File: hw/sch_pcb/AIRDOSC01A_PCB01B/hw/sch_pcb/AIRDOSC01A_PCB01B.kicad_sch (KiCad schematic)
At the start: 39 parts, among them J1 HEADER_2x01_PARALLEL, J10 HEADER_2x01_PARALLEL, J2 HEADER_2x01_PARALLEL, J3 HEADER_2x01_PARALLEL, J4 HEADER_2x01_PARALLEL, J5 HEADER_2x01_PARALLEL, J6 HEADER_2x01_PARALLEL, J7 HEADER_2x01_PARALLEL, J8 HEADER_2x01_PARALLEL, J9 HEADER_2x01_PARALLEL, M1 HOLE, M2 HOLE, M3 HOLE, M4 HOLE, U1 MICROFC-60035-SMT-TR(1), U2 OPA836IDB

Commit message: Přiřazení součástek
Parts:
- C1: UST_ID (none) -> 5c70984812875079b91f8bac
- C2: UST_ID (none) -> 5c70984712875079b91f8b9b
- C3: UST_ID (none) -> 5c70984412875079b91f8867
- C4, C7: UST_ID (none) -> 5c70984712875079b91f8b53
- C5, C8: UST_ID (none) -> 5c70984712875079b91f8b4c
- C6, C9: UST_ID (none) -> 5c70984712875079b91f8b49
- D1: UST_ID (none) -> 5c70984512875079b91f88ac
- R1, R10, R12, R9: UST_ID (none) -> 5c70984512875079b91f898c
- R11, R5, R6: UST_ID (none) -> 5c70984512875079b91f896b
- R2, R4: UST_ID (none) -> 5c70984512875079b91f896d
- R3: UST_ID (none) -> 5c70984512875079b91f8977
- R7, R8: UST_ID (none) -> 5c70984512875079b91f898f

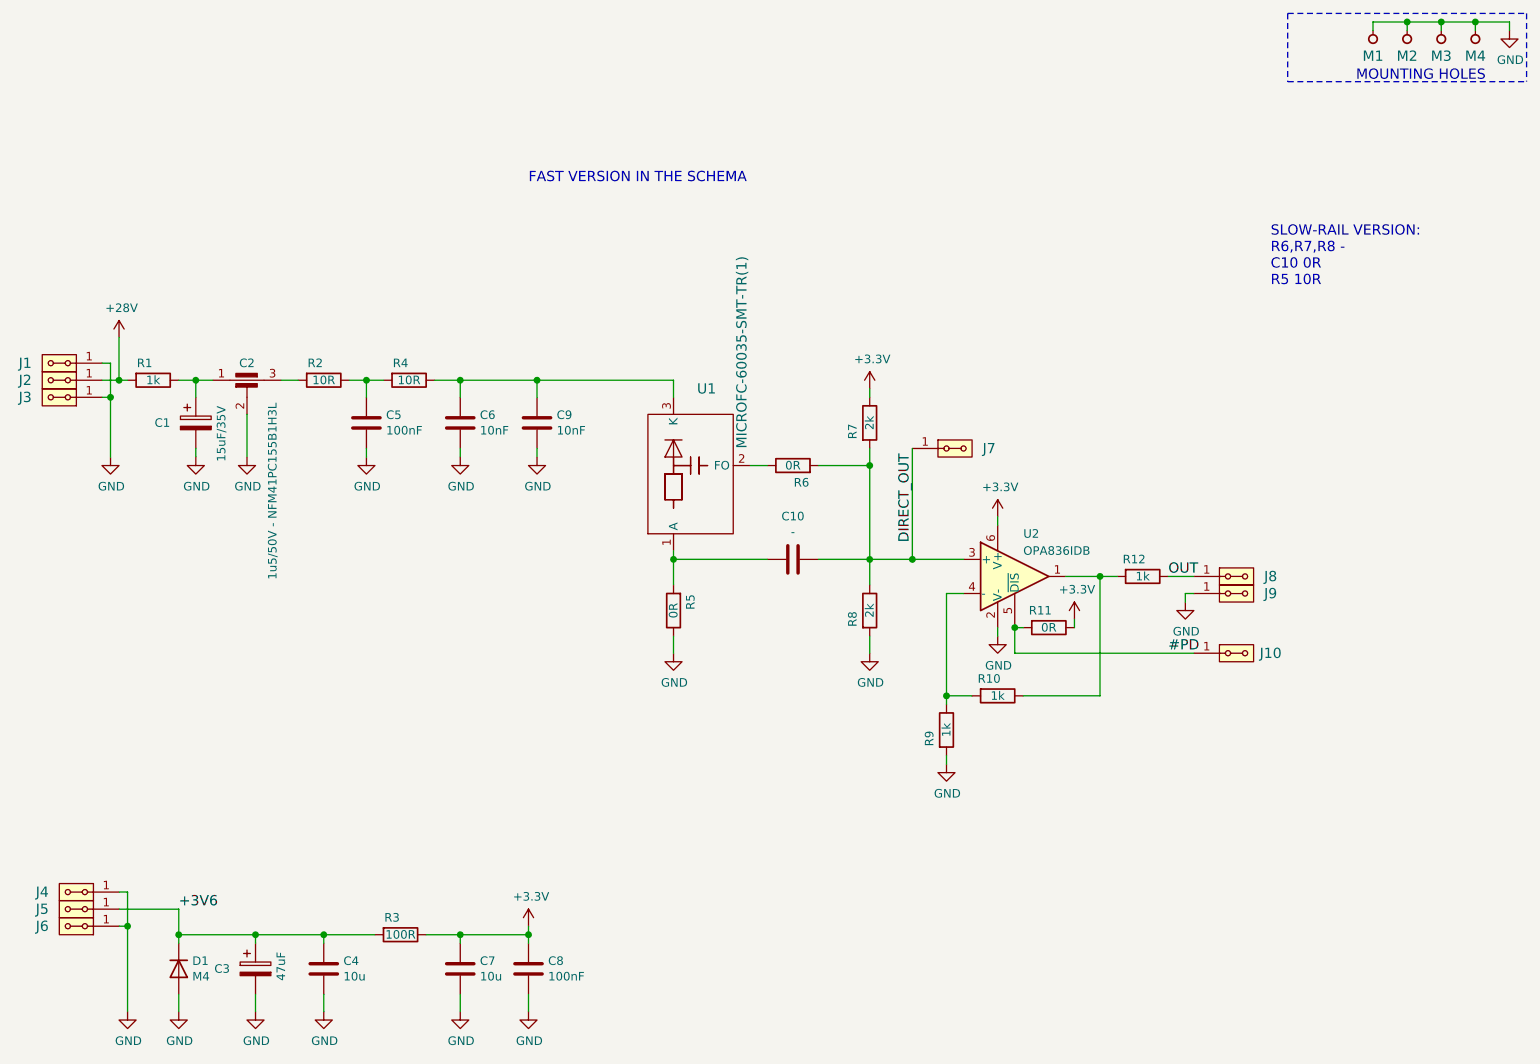
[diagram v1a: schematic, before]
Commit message: Úprava hodnot ve schématu.
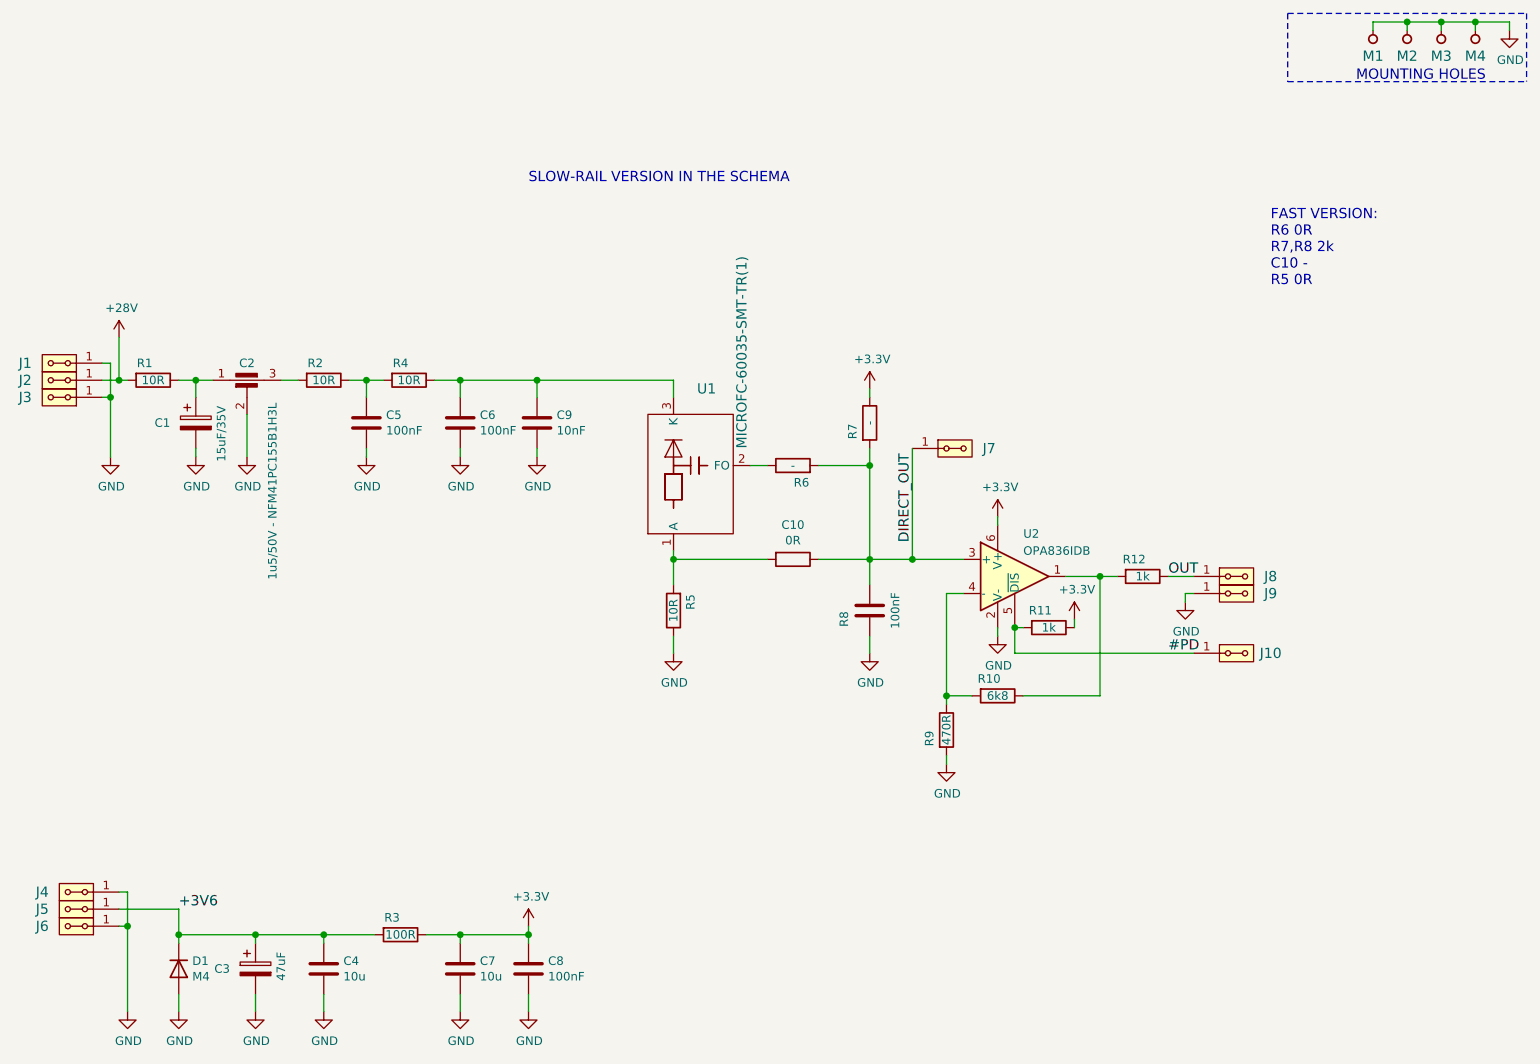
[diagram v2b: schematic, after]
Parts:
- C10: value - -> 0R; symbol Device:C -> Device:R; UST_ID (none) -> 5c70984512875079b91f896b
- C6: value 10nF -> 100nF; UST_ID 5c70984712875079b91f8b49 -> 5c70984712875079b91f8b4c
- R1: value 1k -> 10R; UST_ID 5c70984512875079b91f898c -> 5c70984512875079b91f896d
- R10: value 1k -> 6k8; UST_ID 5c70984512875079b91f898c -> 5c70984612875079b91f899a
- R11: value 0R -> 1k; UST_ID 5c70984512875079b91f896b -> 5c70984512875079b91f898c
- R5: value 0R -> 10R; UST_ID 5c70984512875079b91f896b -> 5c70984512875079b91f896d
- R6: value 0R -> -; UST_ID 5c70984512875079b91f896b -> (none)
- R7: value 2k -> -; UST_ID 5c70984512875079b91f898f -> (none)
- R8: value 2k -> 100nF; symbol Device:R -> Device:C; UST_ID 5c70984512875079b91f898f -> 5c70984712875079b91f8b4c
- R9: value 1k -> 470R; UST_ID 5c70984512875079b91f898c -> 5c70984512875079b91f8986
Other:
- note added: "FAST VERSION: R6 0R R7,R8 2k C10 - R5 0R"
- note added: "SLOW-RAIL VERSION IN THE SCHEMA"
- note removed: "FAST VERSION IN THE SCHEMA"
- note removed: "SLOW-RAIL VERSION: R6,R7,R8 - C10 0R R5 10R"
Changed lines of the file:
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@@
     (stroke (width 0) (type dash) (color 0 0 0 0))
   )
-  (text "FAST VERSION IN THE SCHEMA" (at 133.35 39.37 0)
+  (text "SLOW-RAIL VERSION IN THE SCHEMA" (at 133.35 39.37 0)
     (effects (font (size 1.524 1.524)) (justify left bottom))
   )
-  (text "SLOW-RAIL VERSION:\nR6,R7,R8 -\nC10 0R\nR5 10R\n\n" (at 243.84 57.15 0)
+  (text "FAST VERSION:\nR6 0R\nR7,R8 2k\nC10 -\nR5 0R\n\n" (at 243.84 57.15 0)
     (effects (font (size 1.524 1.524)) (justify left bottom))
   )
@@
     (in_bom yes) (on_board yes)
     (property "Reference" "R1" (id 0) (at 76.2 66.04 90))
-    (property "Value" "1k" (id 1) (at 77.47 68.58 90))
+    (property "Value" "10R" (id 1) (at 77.47 68.58 90))
     (property "Footprint" "Mlab_R:SMD-0805" (id 2) (at 77.47 66.802 90)
       (effects (font (size 1.27 1.27)) hide)
@@
       (effects (font (size 1.27 1.27)) hide)
     )
-    (property "UST_ID" "5c70984512875079b91f898c" (id 4) (at 77.47 68.58 0)
+    (property "UST_ID" "5c70984512875079b91f896d" (id 4) (at 77.47 68.58 0)
       (effects (font (size 1.27 1.27)) hide)
     )
@@
     (in_bom yes) (on_board yes)
     (property "Reference" "R5" (id 0) (at 157.48 101.6 90))
-    (property "Value" "0R" (id 1) (at 154.94 102.87 90))
+    (property "Value" "10R" (id 1) (at 154.94 102.87 90))
     (property "Footprint" "Mlab_R:SMD-0805" (id 2) (at 156.718 102.87 90)
       (effects (font (size 1.27 1.27)) hide)
@@
       (effects (font (size 1.27 1.27)) hide)
     )
-    (property "UST_ID" "5c70984512875079b91f896b" (id 4) (at 154.94 102.87 0)
+    (property "UST_ID" "5c70984512875079b91f896d" (id 4) (at 154.94 102.87 0)
       (effects (font (size 1.27 1.27)) hide)
     )
@@
     (in_bom yes) (on_board yes)
     (property "Reference" "R6" (id 0) (at 173.99 83.82 90))
-    (property "Value" "0R" (id 1) (at 172.72 81.28 90))
+    (property "Value" "-" (id 1) (at 172.72 81.28 90))
     (property "Footprint" "Mlab_R:SMD-0805" (id 2) (at 172.72 83.058 90)
       (effects (font (size 1.27 1.27)) hide)
@@
       (effects (font (size 1.27 1.27)) hide)
     )
-    (property "UST_ID" "5c70984512875079b91f896b" (id 4) (at 172.72 81.28 0)
+    (property "UST_ID" "" (id 4) (at 172.72 81.28 0)
+      (effects (font (size 1.27 1.27)) hide)
+    )
+    (pin "1")
+    (pin "2")
+  )
+  (symbol (lib_id "Device:R") (at 172.72 95.25 270) (unit 1)
+    (in_bom yes) (on_board yes)
+    (property "Reference" "C10" (id 0) (at 172.72 90.1192 90))
+    (property "Value" "0R" (id 1) (at 172.72 92.431 90))
+    (property "Footprint" "Mlab_R:SMD-0805" (id 2) (at 172.72 93.472 90)
+      (effects (font (size 1.27 1.27)) hide)
+    )
+    (property "Datasheet" "~" (id 3) (at 172.72 95.25 0)
+      (effects (font (size 1.27 1.27)) hide)
+    )
+    (property "UST_ID" "5c70984512875079b91f896b" (id 4) (at 172.72 95.25 0)
       (effects (font (size 1.27 1.27)) hide)
     )
@@
     (in_bom yes) (on_board yes)
     (property "Reference" "R7" (id 0) (at 181.61 76.2 90))
-    (property "Value" "2k" (id 1) (at 184.15 74.93 90))
+    (property "Value" "-" (id 1) (at 184.15 74.93 90))
     (property "Footprint" "Mlab_R:SMD-0805" (id 2) (at 182.372 74.93 90)
       (effects (font (size 1.27 1.27)) hide)
@@
       (effects (font (size 1.27 1.27)) hide)
     )
-    (property "UST_ID" "5c70984512875079b91f898f" (id 4) (at 184.15 74.93 0)
-      (effects (font (size 1.27 1.27)) hide)
-    )
-    (pin "1")
-    (pin "2")
-  )
-  (symbol (lib_id "Device:R") (at 184.15 102.87 0) (unit 1)
-    (in_bom yes) (on_board yes)
-    (property "Reference" "R8" (id 0) (at 181.61 104.14 90))
-    (property "Value" "2k" (id 1) (at 184.15 102.87 90))
-    (property "Footprint" "Mlab_R:SMD-0805" (id 2) (at 182.372 102.87 90)
-      (effects (font (size 1.27 1.27)) hide)
-    )
-    (property "Datasheet" "~" (id 3) (at 184.15 102.87 0)
-      (effects (font (size 1.27 1.27)) hide)
-    )
-    (property "UST_ID" "5c70984512875079b91f898f" (id 4) (at 184.15 102.87 0)
+    (property "UST_ID" "" (id 4) (at 184.15 74.93 0)
       (effects (font (size 1.27 1.27)) hide)
     )
@@
     (in_bom yes) (on_board yes)
     (property "Reference" "R9" (id 0) (at 193.04 121.92 90))
-    (property "Value" "1k" (id 1) (at 195.58 120.65 90))
+    (property "Value" "470R" (id 1) (at 195.58 120.65 90))
     (property "Footprint" "Mlab_R:SMD-0805" (id 2) (at 193.802 120.65 90)
       (effects (font (size 1.27 1.27)) hide)
@@
       (effects (font (size 1.27 1.27)) hide)
     )
-    (property "UST_ID" "5c70984512875079b91f898c" (id 4) (at 195.58 120.65 0)
+    (property "UST_ID" "5c70984512875079b91f8986" (id 4) (at 195.58 120.65 0)
       (effects (font (size 1.27 1.27)) hide)
     )
@@
     (in_bom yes) (on_board yes)
     (property "Reference" "R10" (id 0) (at 201.93 113.03 90))
-    (property "Value" "1k" (id 1) (at 203.2 115.57 90))
+    (property "Value" "6k8" (id 1) (at 203.2 115.57 90))
     (property "Footprint" "Mlab_R:SMD-0805" (id 2) (at 203.2 113.792 90)
       (effects (font (size 1.27 1.27)) hide)
@@
       (effects (font (size 1.27 1.27)) hide)
     )
-    (property "UST_ID" "5c70984512875079b91f898c" (id 4) (at 203.2 115.57 0)
+    (property "UST_ID" "5c70984612875079b91f899a" (id 4) (at 203.2 115.57 0)
       (effects (font (size 1.27 1.27)) hide)
     )
@@
     (in_bom yes) (on_board yes)
     (property "Reference" "R11" (id 0) (at 209.55 102.87 90))
-    (property "Value" "0R" (id 1) (at 210.82 105.41 90))
+    (property "Value" "1k" (id 1) (at 210.82 105.41 90))
     (property "Footprint" "Mlab_R:SMD-0805" (id 2) (at 210.82 103.632 90)
       (effects (font (size 1.27 1.27)) hide)
@@
       (effects (font (size 1.27 1.27)) hide)
     )
-    (property "UST_ID" "5c70984512875079b91f896b" (id 4) (at 210.82 105.41 0)
+    (property "UST_ID" "5c70984512875079b91f898c" (id 4) (at 210.82 105.41 0)
       (effects (font (size 1.27 1.27)) hide)
     )
@@
       (effects (font (size 1.27 1.27)) (justify left))
     )
-    (property "Value" "10nF" (id 1) (at 126.111 76.073 0)
+    (property "Value" "100nF" (id 1) (at 126.111 76.073 0)
       (effects (font (size 1.27 1.27)) (justify left))
     )
@@
       (effects (font (size 1.27 1.27)) hide)
     )
-    (property "UST_ID" "5c70984712875079b91f8b49" (id 4) (at 123.19 74.93 0)
+    (property "UST_ID" "5c70984712875079b91f8b4c" (id 4) (at 123.19 74.93 0)
       (effects (font (size 1.27 1.27)) hide)
     )
@@
     (pin "2")
   )
-  (symbol (lib_id "Device:C") (at 172.72 95.25 270) (unit 1)
-    (in_bom yes) (on_board yes)
-    (property "Reference" "C10" (id 0) (at 172.72 88.8492 90))
-    (property "Value" "-" (id 1) (at 172.72 91.1606 90))
-    (property "Footprint" "Mlab_R:SMD-0805" (id 2) (at 168.91 96.2152 0)
-      (effects (font (size 1.27 1.27)) hide)
-    )
-    (property "Datasheet" "~" (id 3) (at 172.72 95.25 0)
+  (symbol (lib_id "Device:C") (at 184.15 102.87 0) (unit 1)
+    (in_bom yes) (on_board yes)
+    (property "Reference" "R8" (id 0) (at 180.34 104.14 90))
+    (property "Value" "100nF" (id 1) (at 187.96 102.87 90))
+    (property "Footprint" "Mlab_R:SMD-0805" (id 2) (at 185.1152 106.68 0)
+      (effects (font (size 1.27 1.27)) hide)
+    )
+    (property "Datasheet" "~" (id 3) (at 184.15 102.87 0)
+      (effects (font (size 1.27 1.27)) hide)
+    )
+    (property "UST_ID" "5c70984712875079b91f8b4c" (id 4) (at 184.15 102.87 0)
       (effects (font (size 1.27 1.27)) hide)
     )
@@
     )
     (path "/00000000-0000-0000-0000-00005c6c3f27"
-      (reference "C6") (unit 1) (value "10nF") (footprint "Mlab_R:SMD-0805")
+      (reference "C6") (unit 1) (value "100nF") (footprint "Mlab_R:SMD-0805")
     )
     (path "/00000000-0000-0000-0000-00005c7302b4"
@@
     )
     (path "/00000000-0000-0000-0000-00005c6e466e"
-      (reference "C10") (unit 1) (value "-") (footprint "Mlab_R:SMD-0805")
+      (reference "C10") (unit 1) (value "0R") (footprint "Mlab_R:SMD-0805")
     )
     (path "/00000000-0000-0000-0000-00005c742691"
@@
     )
     (path "/00000000-0000-0000-0000-00005c6c24df"
-      (reference "R1") (unit 1) (value "1k") (footprint "Mlab_R:SMD-0805")
+      (reference "R1") (unit 1) (value "10R") (footprint "Mlab_R:SMD-0805")
     )
     (path "/00000000-0000-0000-0000-00005c6c26ca"
@@
     )
     (path "/00000000-0000-0000-0000-00005c6ddfa9"
-      (reference "R5") (unit 1) (value "0R") (footprint "Mlab_R:SMD-0805")
+      (reference "R5") (unit 1) (value "10R") (footprint "Mlab_R:SMD-0805")
     )
     (path "/00000000-0000-0000-0000-00005c6e438b"
-      (reference "R6") (unit 1) (value "0R") (footprint "Mlab_R:SMD-0805")
+      (reference "R6") (unit 1) (value "-") (footprint "Mlab_R:SMD-0805")
     )
     (path "/00000000-0000-0000-0000-00005c6e44ae"
-      (reference "R7") (unit 1) (value "2k") (footprint "Mlab_R:SMD-0805")
+      (reference "R7") (unit 1) (value "-") (footprint "Mlab_R:SMD-0805")
     )
     (path "/00000000-0000-0000-0000-00005c6e4554"
-      (reference "R8") (unit 1) (value "2k") (footprint "Mlab_R:SMD-0805")
+      (reference "R8") (unit 1) (value "100nF") (footprint "Mlab_R:SMD-0805")
     )
     (path "/00000000-0000-0000-0000-00005c6f744a"
-      (reference "R9") (unit 1) (value "1k") (footprint "Mlab_R:SMD-0805")
+      (reference "R9") (unit 1) (value "470R") (footprint "Mlab_R:SMD-0805")
     )
     (path "/00000000-0000-0000-0000-00005c6ff14e"
-      (reference "R10") (unit 1) (value "1k") (footprint "Mlab_R:SMD-0805")
+      (reference "R10") (unit 1) (value "6k8") (footprint "Mlab_R:SMD-0805")
     )
     (path "/00000000-0000-0000-0000-00005c6f9be2"
-      (reference "R11") (unit 1) (value "0R") (footprint "Mlab_R:SMD-0805")
+      (reference "R11") (unit 1) (value "1k") (footprint "Mlab_R:SMD-0805")
     )
     (path "/00000000-0000-0000-0000-00005c70a07b"
